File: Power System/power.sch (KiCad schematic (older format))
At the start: 35 parts, among them J1 PC104_40Pin_2.54mm, J2 Charge Cable, J3 Battery Pack, J4 IDC Header, U1 ds2781e+, U2 LT3461ES6-TRMPBF

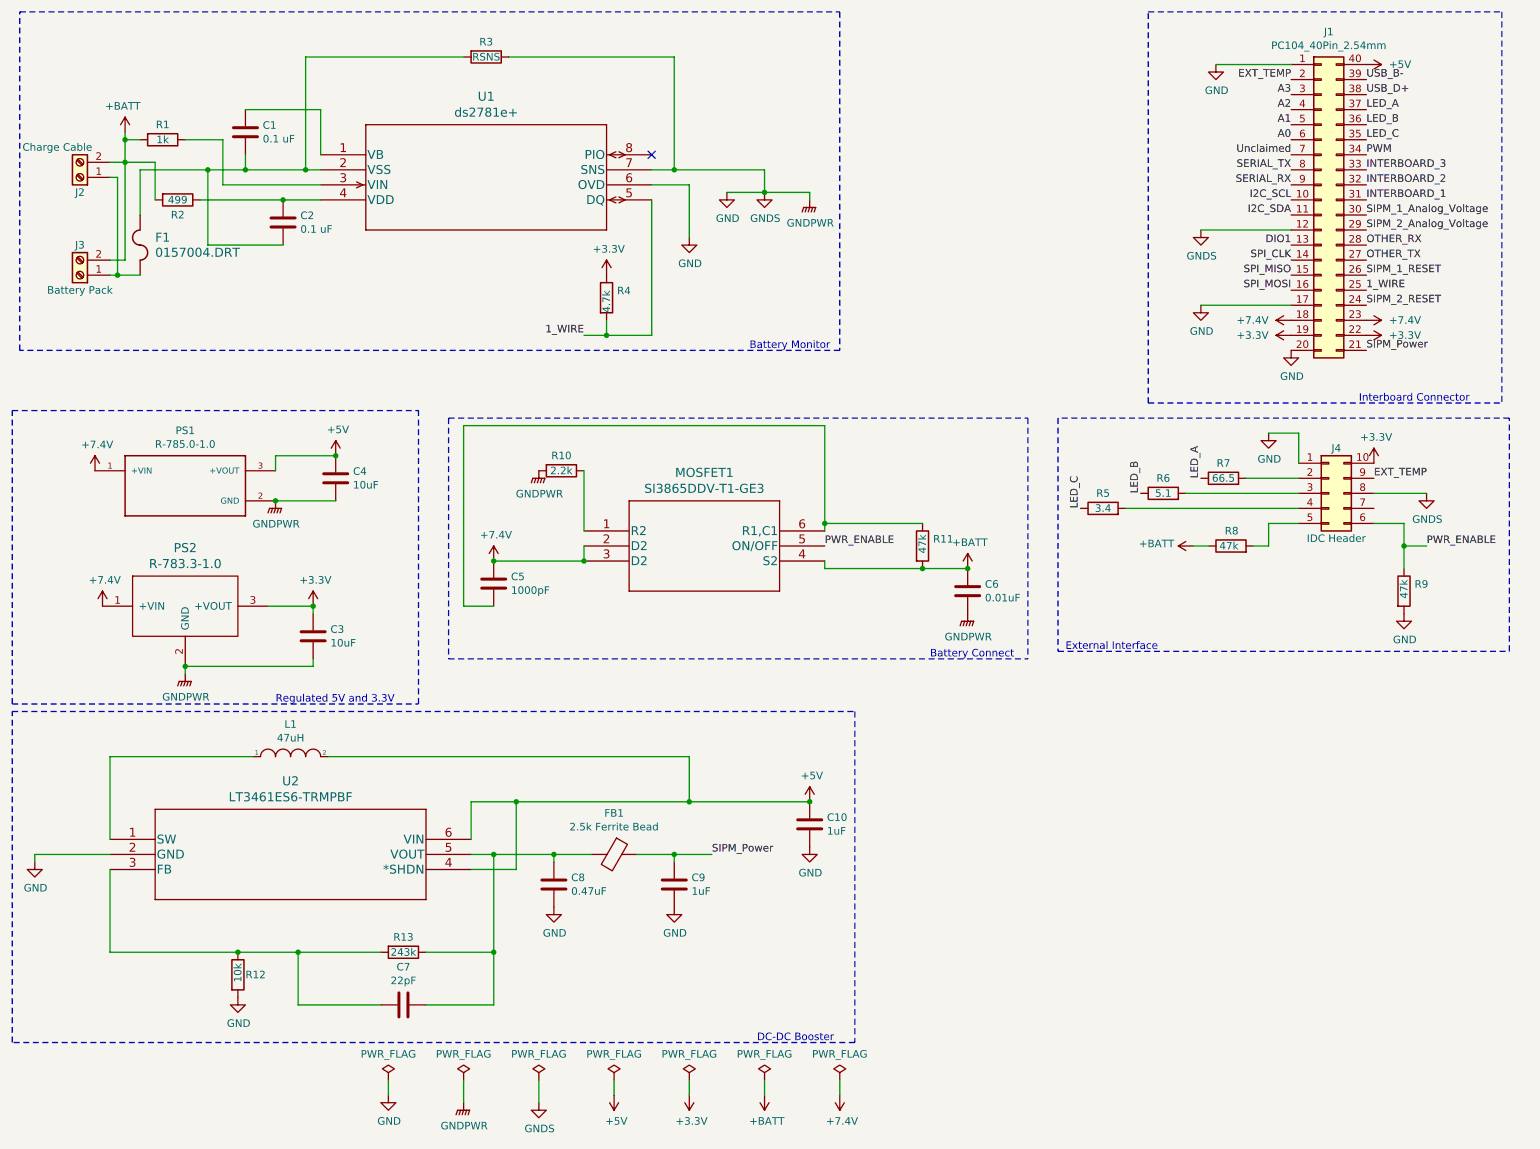
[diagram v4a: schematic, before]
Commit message: Switched some footprints and created gerber files
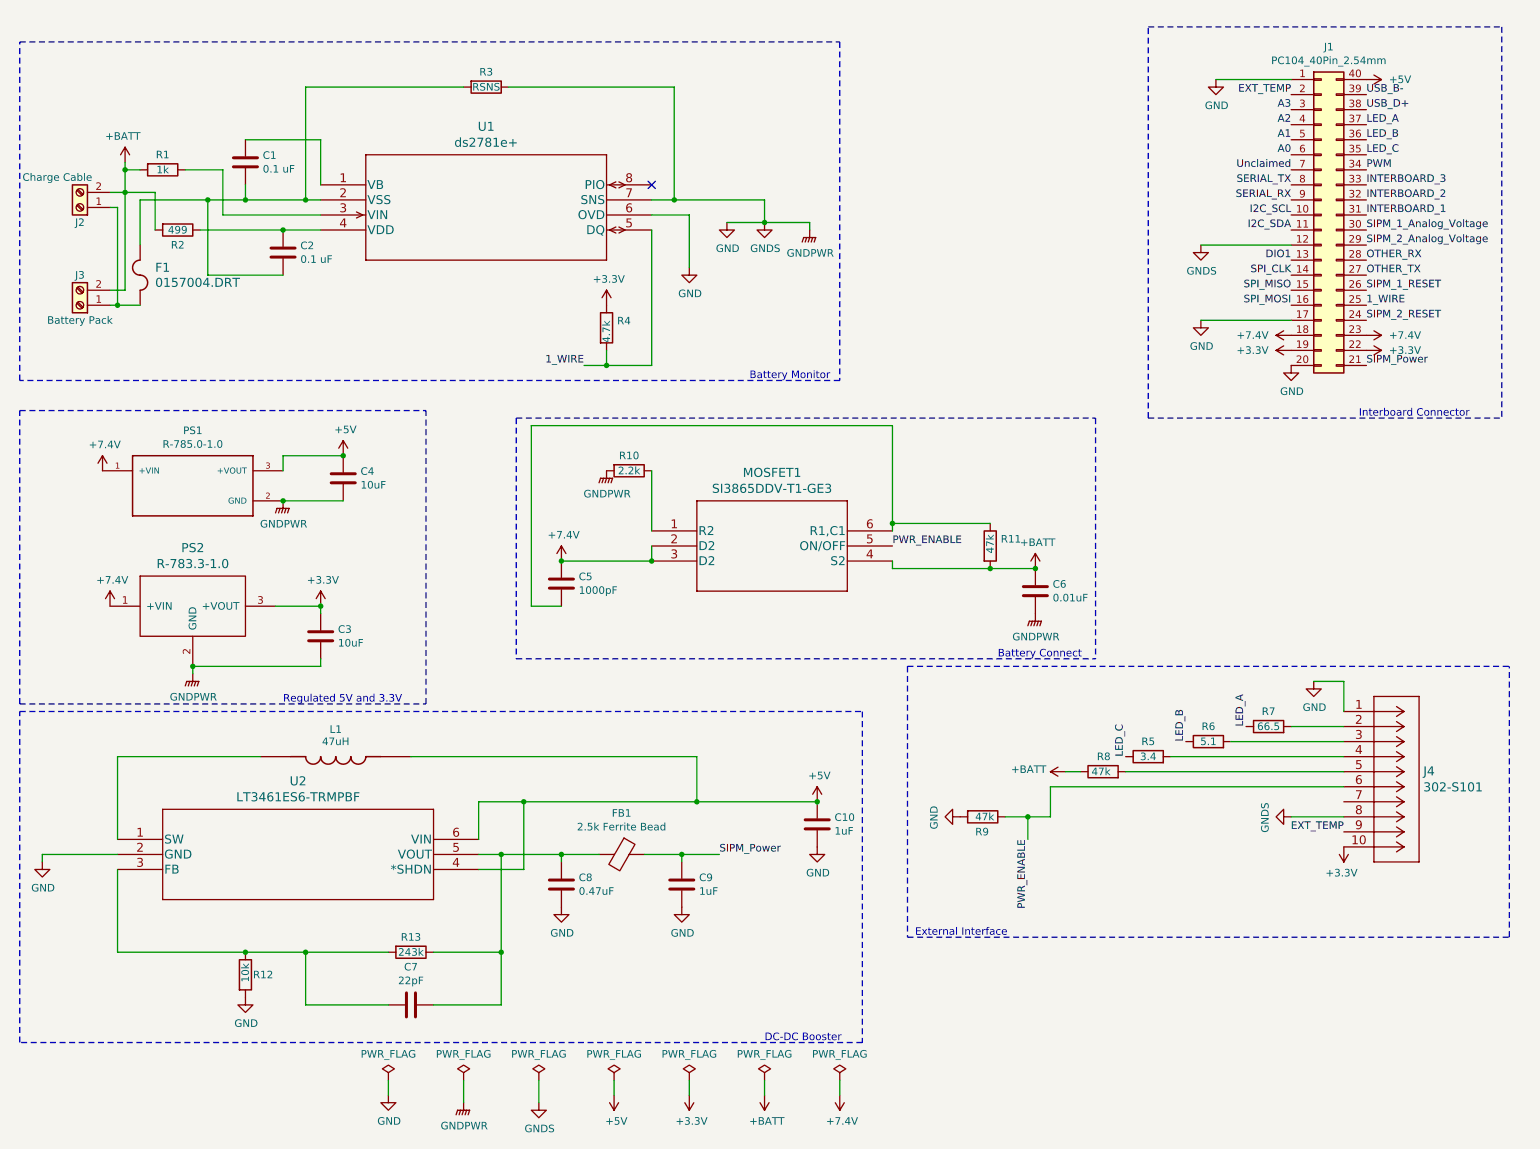
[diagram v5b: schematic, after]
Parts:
- removed J4: IDC Header, Connector_IDC:IDC-Header_2x05_P2.54mm_Vertical, symbol Connector_Generic:Conn_02x05_Counter_Clockwise
- removed L1: 47uH, Inductor_SMD:L_1206_3216Metric_Pad1.22x1.90mm_HandSolder, symbol pspice:INDUCTOR
- added J4: 302-S101, 302-S101Connector:302-S101, symbol 302-S101Connector:302-S101
- added L1: 47uH, LQH43NH470J03L-Inductor:IND_LQH43NH470J03L, symbol LQH43NH470J03L-Inductor:LQH43NH470J03L
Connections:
- net +3V3: now also J4.10
- net +5V: now also L1.2
- net EXT_TEMP: now also J4.9
- net GND: now also J4.1, J4.8
- net PWR_ENABLE: now also J4.6
- net at R7.2: now also J4.2
- net at R6.2: now also J4.3
- net at R5.2: now also J4.4
- net at R8.2: now also J4.5
- net at U2.1 (SW): now also L1.1
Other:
- moved on the sheet: C1, C10, C2, C3, C4, C5, C6, C7, C8, C9, F1, FB1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
